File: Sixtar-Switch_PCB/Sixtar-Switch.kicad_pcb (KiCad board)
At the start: 2 copper layers, 73 parts, among them J1 USB_C_Receptacle, SW1 RUN, SW2 USB_Boot, U1 AMS1117-3.3, U2 RP2040, U3 W25Q128JVS, Y1 12.000MHz(ATS,SMD)

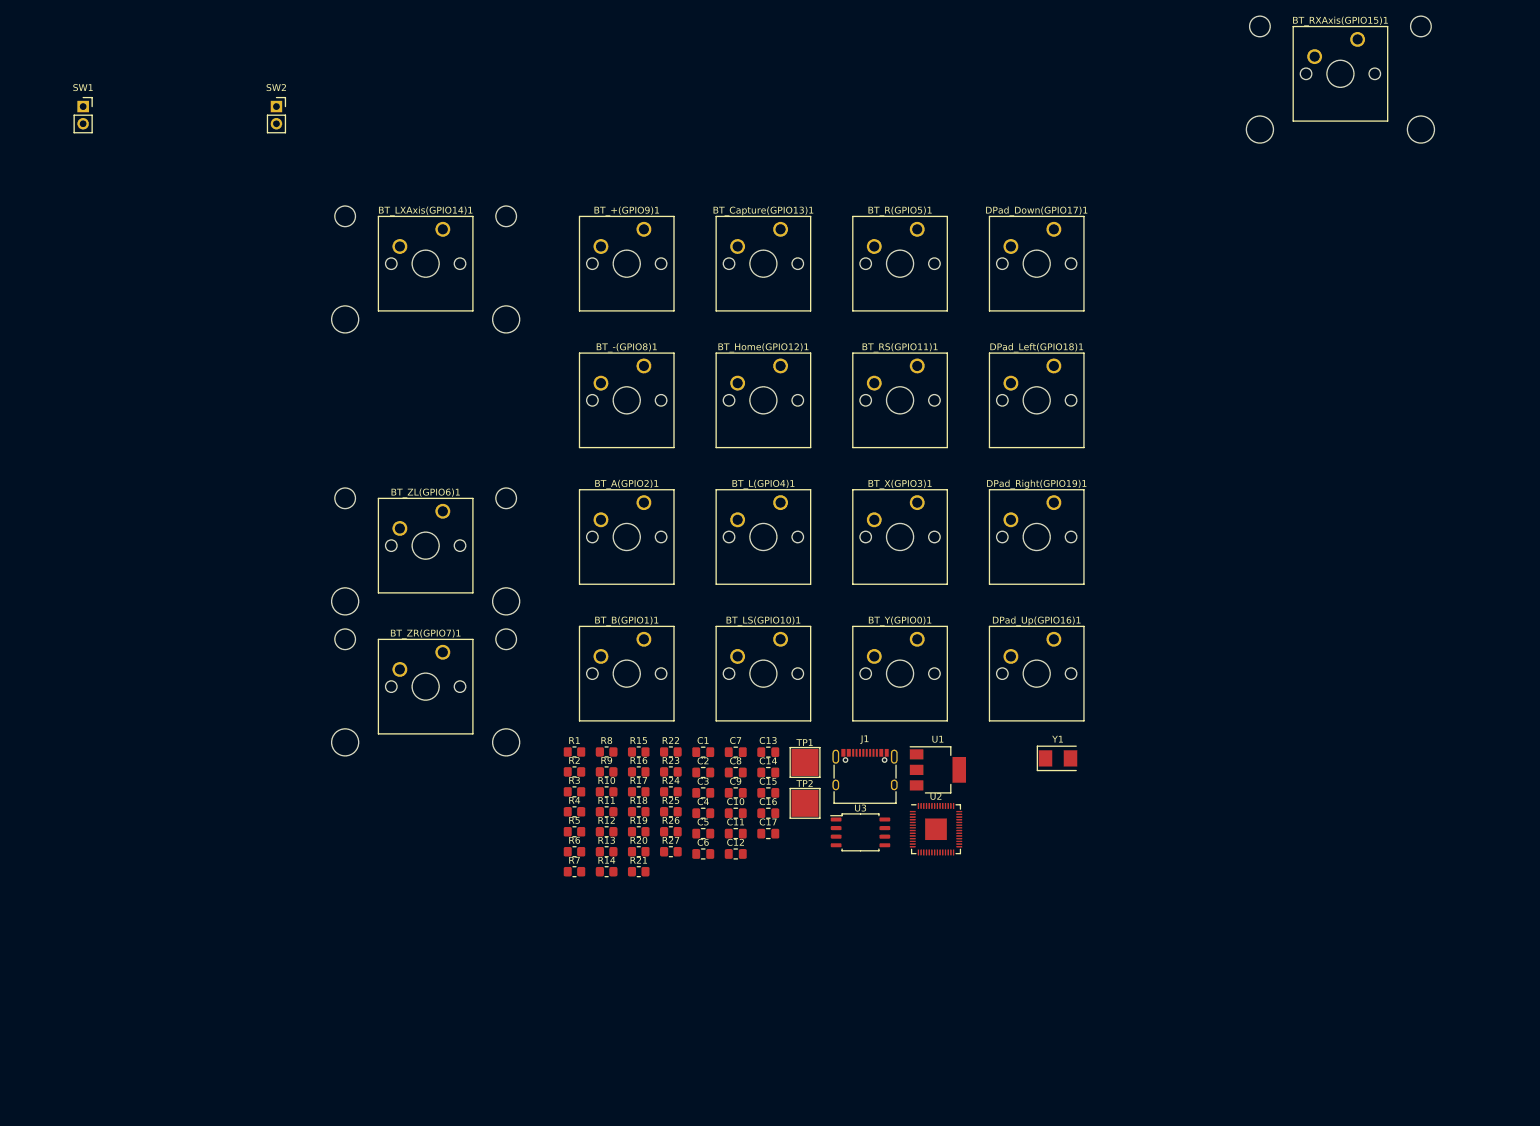
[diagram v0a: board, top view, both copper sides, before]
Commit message: KiCAD 회로 수정 및 PCB 제작중
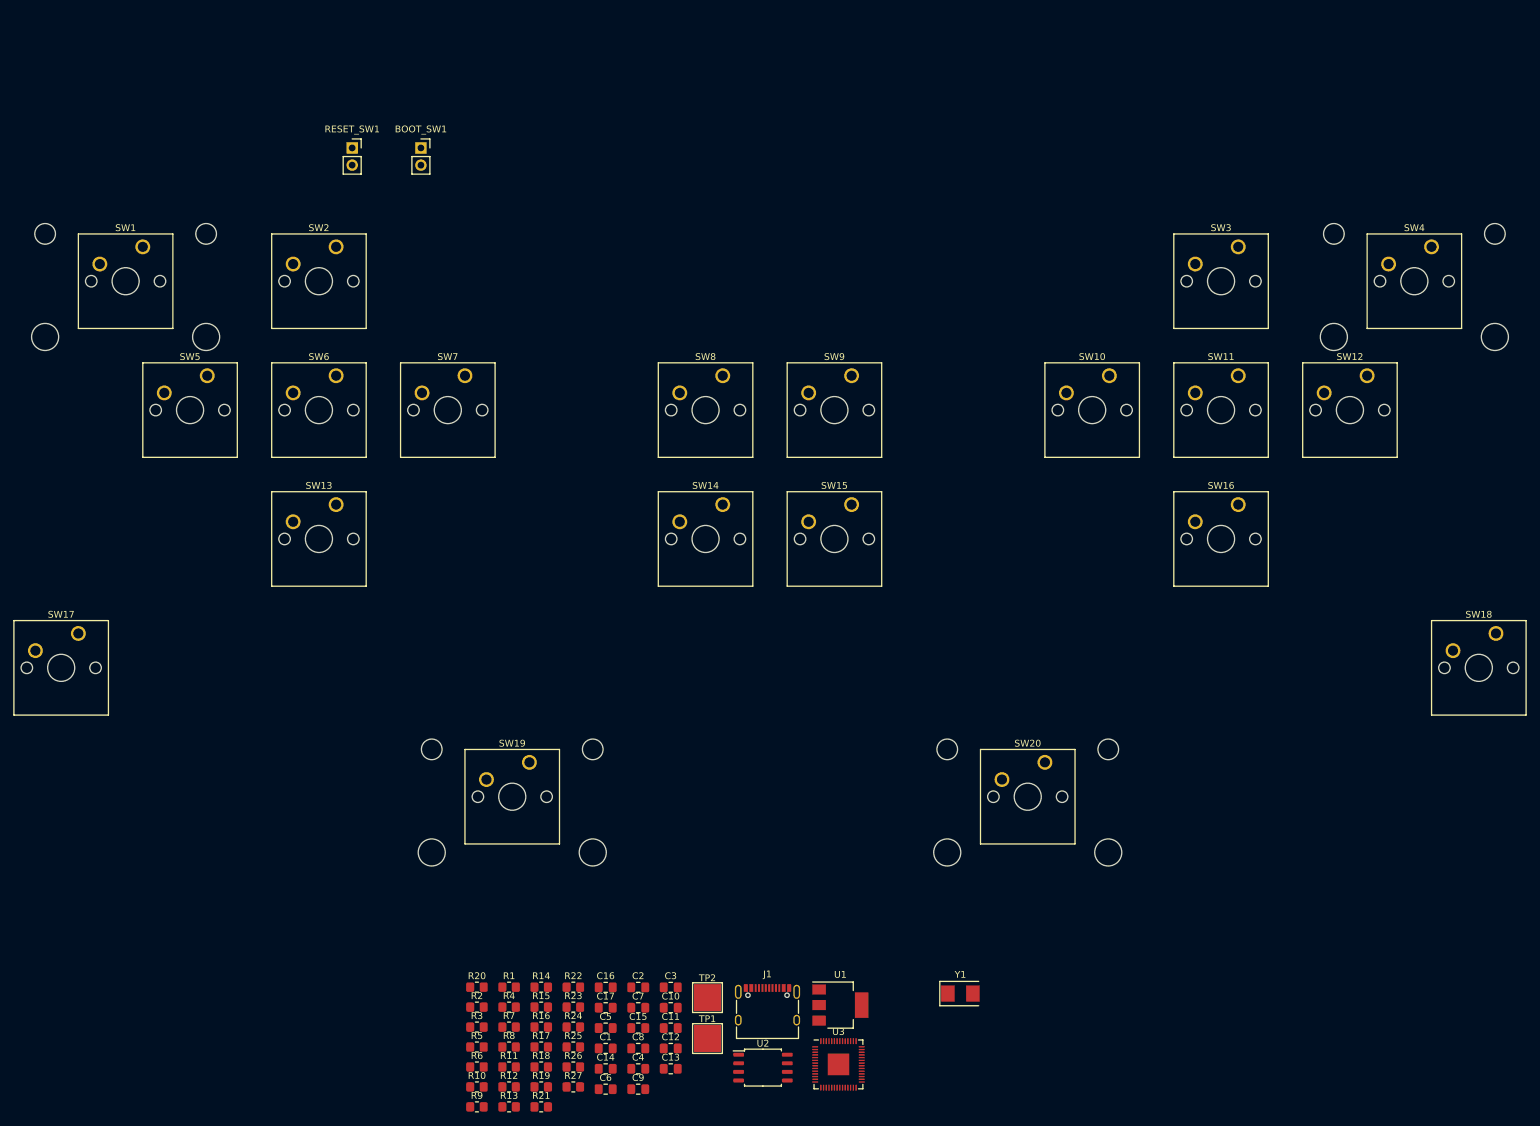
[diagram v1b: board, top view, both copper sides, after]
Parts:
- moved SW5 125.2 mm to (62.4, 74.3)
- moved SW2 120.9 mm to (81.4, 55.3)
- moved SW17 119.8 mm to (43.3, 112.4)
- moved SW13 113.6 mm to (81.4, 93.4)
- moved SW18 112.9 mm to (252.9, 112.4)
- moved SW12 108.5 mm to (233.8, 74.3)
- moved SW20 90.5 mm to (186.2, 131.5)
- moved SW16 90.1 mm to (214.8, 93.4)
- moved SW7 89.0 mm to (100.5, 74.3)
- moved SW6 76.4 mm to (81.4, 74.3)
- moved SW3 60.7 mm to (214.8, 55.3)
- moved SW15 51.0 mm to (157.6, 93.4)
- moved SW10 48.2 mm to (195.7, 74.3)
- moved SW11 47.5 mm to (214.8, 74.3)
- moved SW1 44.4 mm to (52.9, 55.3)
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- renumbered SW2 to BOOT_SW1, C4 to C1, C14 to C10, C15 to C11, C16 to C12, C17 to C13, C5 to C14, C9 to C15, C1 to C16, C2 to C17, C7 to C2, C13 to C3, C11 to C4, C3 to C5, C8 to C7, C10 to C8, C12 to C9, R8 to R1, R6 to R10, R12 to R11, R13 to R12, R14 to R13, R15 to R14, R16 to R15, R17 to R16, R18 to R17, R19 to R18, R20 to R19, R1 to R20, R9 to R4, R4 to R5, R5 to R6, R10 to R7, R11 to R8, R7 to R9, SW1 to RESET_SW1, BT_LXAxis(GPIO14)1 to SW1, BT_Y(GPIO0)1 to SW10, BT_RS(GPIO11)1 to SW11, BT_A(GPIO2)1 to SW12, DPad_Down(GPIO17)1 to SW13, BT_-(GPIO8)1 to SW14, BT_+(GPIO9)1 to SW15, BT_B(GPIO1)1 to SW16, BT_Capture(GPIO13)1 to SW17, BT_Home(GPIO12)1 to SW18, BT_ZL(GPIO6)1 to SW19, DPad_Up(GPIO16)1 to SW2, BT_ZR(GPIO7)1 to SW20, BT_X(GPIO3)1 to SW3, BT_RXAxis(GPIO15)1 to SW4, DPad_Left(GPIO18)1 to SW5, BT_LS(GPIO10)1 to SW6, DPad_Right(GPIO19)1 to SW7, BT_L(GPIO4)1 to SW8, BT_R(GPIO5)1 to SW9, TP2 to TP1, TP1 to TP2, U3 to U2, U2 to U3

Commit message: 키 배치 수정
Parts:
- moved U3 153.3 mm to (109.8, 29.8)
- moved J1 146.9 mm to (138.0, 21.8), turned to 180 degrees
- moved U1 140.2 mm to (127.0, 30.2)
- moved RESET_SW1 122.1 mm to (134.0, 152.0)
- moved BOOT_SW1 122.1 mm to (144.2, 152.0)
- moved SW2 46.6 mm to (74.0, 28.4)
- moved SW3 46.6 mm to (207.3, 28.4)
- moved SW19 27.9 mm to (102.5, 104.6)
- moved SW20 27.9 mm to (178.7, 104.6)
- moved SW9 27.9 mm to (150.2, 47.4)
- moved SW10 27.9 mm to (188.3, 47.4)
- moved SW12 27.9 mm to (226.4, 47.4)
- moved SW5 27.9 mm to (54.9, 47.4)
- moved SW7 27.9 mm to (93.0, 47.4)
- moved SW8 27.9 mm to (131.1, 47.4)
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- renumbered SW3 to SW11, SW6 to SW2, SW11 to SW3, SW2 to SW6
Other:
- board outline added: 240 x 107 mm

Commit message: 저항 배치중
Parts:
- R1, R11, R12, R13, R14, R15, R16, R17, R18, R19, R2, R21, R22, R23, R24, R25, R26, R27, R3, R4, R7, R8, TP1, TP2: moved to B.Cu
- moved R23 172.1 mm to (229.5, 37.8), turned to 90 degrees
- moved R18 164.9 mm to (200.9, 37.8), turned to 90 degrees
- moved R7 160.3 mm to (219.9, 56.8), turned to 90 degrees
- moved TP1 156.6 mm to (89.8, 22.8), turned to 180 degrees
- moved R6 153.0 mm to (99.3, 23.5)
- moved R19 152.8 mm to (239.0, 94.9), turned to 90 degrees
- moved TP2 152.5 mm to (84.7, 22.8), turned to 180 degrees
- moved R5 152.0 mm to (110.4, 21.8)
- moved R3 151.8 mm to (136.8, 22.8), turned to 90 degrees
- moved R8 149.8 mm to (200.9, 56.8), turned to 90 degrees
- moved U2 149.6 mm to (110.0, 31.0)
- moved R2 149.5 mm to (139.1, 22.8), turned to 90 degrees
- moved R22 148.7 mm to (38.9, 37.8), turned to 90 degrees
- moved R17 142.8 mm to (67.5, 37.8), turned to 90 degrees
- moved R26 137.7 mm to (48.5, 56.8), turned to 90 degrees
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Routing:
- net GND: track 0.00 -> 30.4 mm, vias 0 -> 2
- net VBUS: track 0.00 -> 18.6 mm
- net +3.3V: track 0.00 -> 6.30 mm
- net D-: track 0.00 -> 2.69 mm
- net D+: track 0.00 -> 2.69 mm
- net Net-(J1-CC2): track 0.00 -> 1.90 mm, vias 0 -> 1
- net Net-(J1-CC1): track 0.00 -> 1.73 mm, vias 0 -> 1

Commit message: 저항 배치 및 배선 그리는중
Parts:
- C16, C17, R10, R20, Y1: moved to B.Cu
- moved R9 157.3 mm to (109.9, 24.5)
- moved R10 146.5 mm to (101.8, 26.7), turned to 180 degrees
- moved Y1 134.1 mm to (105.6, 50.1), turned to 180 degrees
- moved R20 124.8 mm to (103.4, 39.9), turned to 180 degrees
- moved C17 124.0 mm to (107.9, 44.4)
- moved C16 121.6 mm to (103.4, 44.4), turned to 180 degrees
- moved R5 6.08 mm to (104.5, 20.4)
- moved R6 5.20 mm to (104.5, 23.3)
- moved BOOT_SW1 3.55 mm to (101.8, 34.0), turned to 180 degrees
- moved R22 0.14 mm to (39.0, 37.8)
- moved R17 0.13 mm to (67.6, 37.8)
- moved R7 0.12 mm to (220.0, 56.8)
- moved R1 0.12 mm to (181.9, 56.8)
- moved R12 0.12 mm to (143.8, 56.8)
- moved R8 0.07 mm to (201.0, 56.8)
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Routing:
- net QSPI_SS: track 0.00 -> 25.3 mm, vias 0 -> 4
- net Net-(U3-XIN): track 0.00 -> 20.7 mm, vias 0 -> 1
- net +3.3V: track 6.30 -> 22.7 mm, vias 0 -> 2
- net Net-(C17-Pad2): track 0.00 -> 12.8 mm, vias 0 -> 2
- net QSPI_SD0: track 0.00 -> 12.2 mm, vias 0 -> 2
- net Net-(U3-XOUT): track 0.00 -> 12.2 mm, vias 0 -> 1
- net QSPI_SCLK: track 0.00 -> 11.7 mm, vias 0 -> 2
- net QSPI_SD3: track 0.00 -> 7.11 mm, vias 0 -> 1
- net BTN_Minus: track 0.00 -> 5.98 mm
- net DPad_Down: track 0.00 -> 5.96 mm
- net BTN_Plus: track 0.00 -> 5.96 mm
- net BTN_ZL: track 0.00 -> 5.95 mm
- net BTN_B: track 0.00 -> 5.94 mm
- net BTN_LXAxis: track 0.00 -> 5.91 mm
- net BTN_RXAxis: track 0.00 -> 5.91 mm
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- added copper zone on B.Cu, net GND
- added copper zone on F.Cu, net GND

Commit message: PCB빌드 완료. 테스트 필요
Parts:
- removed TP1, TP2: TestPoint, TestPoint:TestPoint_Pad_4.0x4.0mm
- added H1: MountingHole, MountingHole:MountingHole_3.2mm_M3, F.Cu at (22.0, 22.0)
- added H2: MountingHole, MountingHole:MountingHole_3.2mm_M3, F.Cu at (254.0, 23.0)
- added H3: MountingHole, MountingHole:MountingHole_3.2mm_M3, F.Cu at (22.0, 121.0)
- added H4: MountingHole, MountingHole:MountingHole_3.2mm_M3, F.Cu at (254.0, 121.0)
- C10, C11, C12, C13, C14, C15, C5, C6, C7, C8, C9, R5, R6: moved to B.Cu
- R10: moved to F.Cu
- moved C1 145.7 mm to (138.0, 29.1)
- moved C2 129.5 mm to (144.6, 36.5), turned to 90 degrees
- moved C3 128.2 mm to (131.5, 36.5), turned to 90 degrees
- moved R10 101.0 mm to (143.8, 118.5), turned to 0 degrees
- moved C14 95.9 mm to (137.7, 82.2), turned to 180 degrees
- moved BOOT_SW1 95.8 mm to (139.9, 121.9)
- moved C9 95.3 mm to (149.3, 87.4), turned to 180 degrees
- moved C6 94.7 mm to (128.3, 85.3), turned to 180 degrees
- moved C8 91.4 mm to (149.3, 85.4), turned to 180 degrees
- moved C15 89.8 mm to (141.5, 82.2), turned to 180 degrees
- moved R9 87.9 mm to (135.6, 108.5)
- moved C5 87.7 mm to (128.3, 83.4), turned to 180 degrees
- moved C7 87.5 mm to (149.3, 83.4), turned to 180 degrees
- moved U2 86.2 mm to (138.4, 112.4)
- moved C13 83.4 mm to (149.3, 95.4), turned to 180 degrees
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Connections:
- U3 pad 24: Net-(U3-SWCLK) -> unconnected-(U3-SWCLK-Pad24)
- U3 pad 25: Net-(U3-SWD) -> unconnected-(U3-SWD-Pad25)
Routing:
- net GND: track 34.2 -> 860.2 mm, vias 3 -> 12
- net +3.3V: track 22.7 -> 712.6 mm, vias 2 -> 33
- net BTN_RXAxis: track 5.91 -> 210.7 mm, vias 0 -> 10
- net BTN_LXAxis: track 5.91 -> 170.4 mm, vias 0 -> 6
- net BTN_Home: track 0.00 -> 163.4 mm, vias 0 -> 2
- net DPad_Up: track 5.91 -> 149.1 mm, vias 0 -> 8
- net DPad_Left: track 5.89 -> 148.3 mm, vias 0 -> 8
- net BTN_LS: track 5.90 -> 140.1 mm, vias 0 -> 4
- net BTN_RS: track 5.91 -> 130.4 mm, vias 0 -> 10
- net BTN_A: track 5.84 -> 126.5 mm, vias 0 -> 4
- net BTN_Capture: track 5.91 -> 125.8 mm, vias 0 -> 4
- net DPad_Right: track 5.89 -> 116.6 mm, vias 0 -> 8
- net DPad_Down: track 5.96 -> 115.6 mm, vias 0 -> 6
- net BTN_X: track 5.85 -> 111.8 mm, vias 0 -> 4
- net BTN_B: track 5.94 -> 93.2 mm, vias 0 -> 4
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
